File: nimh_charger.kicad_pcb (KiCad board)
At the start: 2 copper layers, 28 parts, among them J1 USB_B_Micro, J2 Bat +, J3 Bat -, Q1 Q_PMOS_DGS, Q2 2N2219, Q3 Q_PMOS_DGS, Q4 Q_PMOS_DGS, U1 LM317L_TO92, U2 LM339

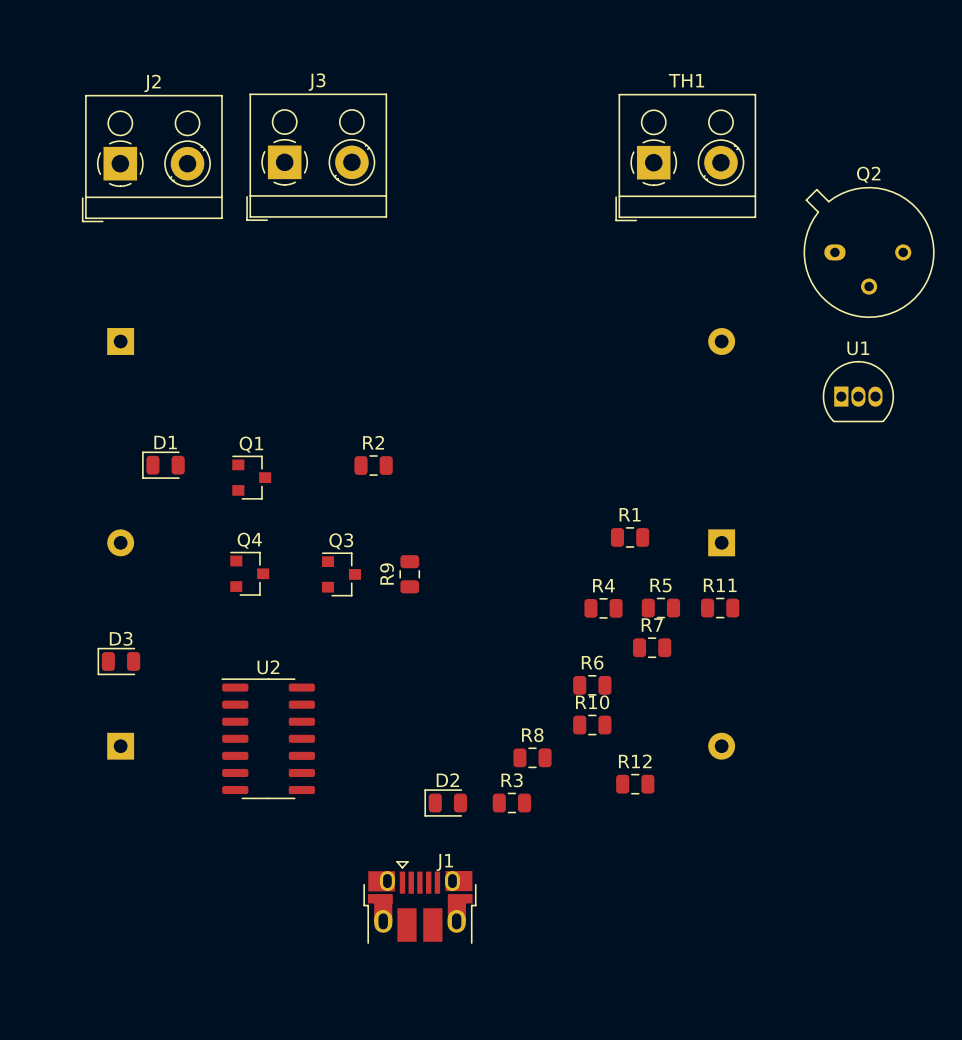
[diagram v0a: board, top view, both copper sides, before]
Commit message: Sorted out some footprints. Working on layout and placement.
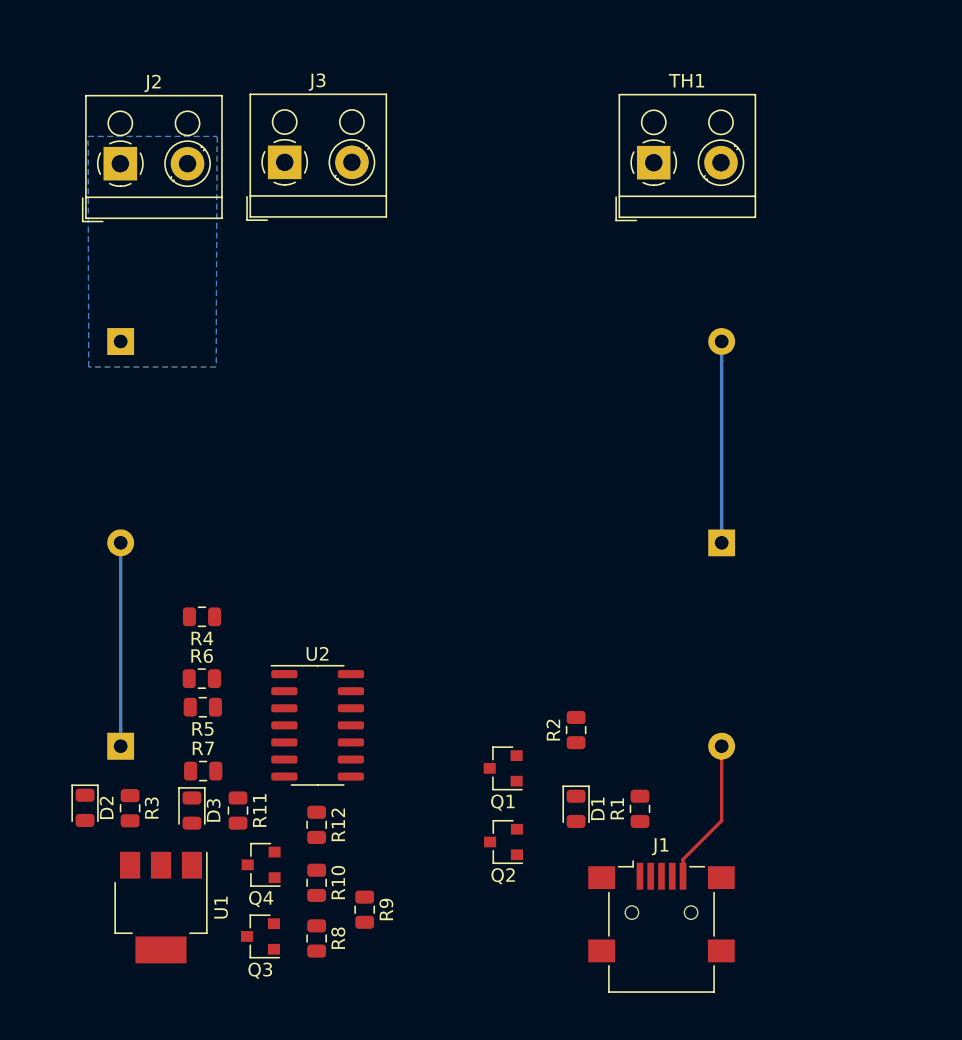
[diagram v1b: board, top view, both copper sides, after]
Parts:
- J1: value USB_B_Micro -> USB_B_Mini; footprint Connector_USB:USB_Micro-B_Amphenol_10103594-0001LF_Horizontal -> Connector_USB:USB_Mini-B_Lumberg_2486_01_Horizontal
- Q2: footprint Package_TO_SOT_THT:TO-39-3 -> Package_TO_SOT_SMD:SOT-23
- U1: value LM317L_TO92 -> LM317_3PinPackage; footprint Package_TO_SOT_THT:TO-92_Inline -> Package_TO_SOT_SMD:SOT-223-3_TabPin2
- moved U1 63.3 mm to (101.2, 115.8), turned to 270 degrees
- moved Q2 50.3 mm to (126.7, 111.0), turned to 180 degrees
- moved D1 39.8 mm to (132.1, 108.5), turned to 270 degrees
- moved R11 38.9 mm to (107.0, 108.6), turned to 270 degrees
- moved R5 34.9 mm to (104.3, 101.0), turned to 180 degrees
- moved R7 34.6 mm to (104.4, 105.7)
- moved R4 29.9 mm to (104.3, 94.2), turned to 180 degrees
- moved R6 29.0 mm to (104.3, 98.8)
- moved Q1 28.6 mm to (126.7, 105.5), turned to 180 degrees
- moved R3 28.4 mm to (98.9, 108.5), turned to 270 degrees
- moved Q3 27.6 mm to (108.6, 118.0), turned to 180 degrees
- moved D2 27.0 mm to (95.6, 108.4), turned to 270 degrees
- moved R9 25.2 mm to (116.4, 116.0), turned to 270 degrees
- moved R2 24.8 mm to (132.1, 102.7), turned to 90 degrees
- moved R12 23.9 mm to (112.8, 109.7), turned to 270 degrees
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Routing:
- net CHR_O: track 0.00 -> 15.1 mm
- net Net-(BT1-Pad2): track 0.00 -> 15.0 mm
- net GNDREF: track 0.00 -> 10.9 mm
- added copper zone on B.Cu, net BAT_V

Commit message: review the design
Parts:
- moved R12 32.2 mm to (133.3, 84.9)
- moved R10 31.8 mm to (133.3, 89.7)
- moved R8 31.8 mm to (133.3, 93.8)
- moved Q3 31.0 mm to (113.9, 87.5)
- moved R11 29.3 mm to (127.5, 87.8)
- moved Q4 28.9 mm to (123.3, 87.8)
- moved R9 28.6 mm to (118.2, 87.5)
- moved D2 18.6 mm to (112.1, 116.9), turned to 90 degrees
- moved U1 16.3 mm to (117.5, 115.6)
- moved R3 13.9 mm to (112.1, 112.8), turned to 90 degrees
- moved D3 12.8 mm to (116.1, 105.9)
- moved Q2 12.1 mm to (136.3, 103.6)
- moved U2 8.09 mm to (119.6, 97.8)
- moved R6 6.73 mm to (110.9, 97.8)
- moved R4 6.72 mm to (110.9, 93.2)
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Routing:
- net BAT_V: track 0.00 -> 87.6 mm, vias 0 -> 2
- net Net-(Q2-Pad2): track 0.00 -> 52.7 mm
- net Net-(D3-Pad2): track 0.00 -> 49.8 mm, vias 0 -> 3
- net +5V: track 0.00 -> 43.8 mm, vias 0 -> 2
- net CHR_O: track 15.1 -> 51.0 mm, vias 0 -> 2
- net Net-(R8-Pad2): track 0.00 -> 34.1 mm, vias 0 -> 2
- net Net-(Q3-Pad3): track 0.00 -> 30.1 mm
- net ~SLOW~: track 0.00 -> 26.8 mm, vias 0 -> 2
- net Net-(Q3-Pad1): track 0.00 -> 22.4 mm
- net Net-(Q1-Pad3): track 0.00 -> 19.8 mm, vias 0 -> 2
- net ~TRK~: track 0.00 -> 16.9 mm, vias 0 -> 2
- net CHG: track 0.00 -> 14.7 mm, vias 0 -> 1
- net Net-(R5-Pad1): track 0.00 -> 9.95 mm
- net Net-(R4-Pad1): track 0.00 -> 9.88 mm
- net GNDREF: track 10.9 -> 20.5 mm, vias 0 -> 5
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- added copper zone on B.Cu, net GNDREF

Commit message: Added some mounting holes
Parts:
- added H1: MountingHole, MountingHole:MountingHole_3mm, F.Cu at (126.1, 60.6)
- added H2: MountingHole, MountingHole:MountingHole_3mm, F.Cu at (97.8, 118.9)
- moved J3 0.10 mm to (110.4, 60.5)
- moved TH1 0.07 mm to (137.9, 60.5)
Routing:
- added copper zone on F.Cu, net Net-(J1-Pad6)
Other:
- board outline added: 52.6 x 67.2 mm
- board text added: "B+"
- board text added: "B-"
- board text added: "NiMH Battery Charger v0.1"
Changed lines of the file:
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@@
   (general
     (thickness 1.6)
-    (drawings 0)
+    (drawings 7)
     (tracks 194)
     (zones 0)
-    (modules 28)
+    (modules 30)
     (nets 23)
   )
@@
     (mod_text_size 1 1)
     (mod_text_width 0.15)
-    (pad_size 1.524 1.524)
-    (pad_drill 0.762)
+    (pad_size 3 3)
+    (pad_drill 3)
     (pad_to_mask_clearance 0.051)
     (solder_mask_min_width 0.25)
@@
     (descr "terminal block RND 205-00001, 2 pins, pitch 5mm, size 10x9mm^2, drill diamater 1.3mm, pad diameter 2.5mm, see http://cdn-reichelt.de/documents/datenblatt/C151/RND_205-00001_DB_EN.pdf, script-generated using https://github.com/pointhi/kicad-footprint-generator/scripts/TerminalBlock_RND")
     (tags "THT terminal block RND 205-00001 pitch 5mm size 10x9mm^2 drill 1.3mm pad 2.5mm")
-    (fp_text reference J2 (at 2.5 -6.06) (layer F.SilkS)
+    (fp_text reference J2 (at 2.5 5.525) (layer F.SilkS)
       (effects (font (size 1 1) (thickness 0.15)))
     )
@@
   )
   (module TerminalBlock_RND:TerminalBlock_RND_205-00001_1x02_P5.00mm_Horizontal (layer F.Cu)
-    (at 110.425 60.425)
+    (at 110.425 60.525)
     (descr "terminal block RND 205-00001, 2 pins, pitch 5mm, size 10x9mm^2, drill diamater 1.3mm, pad diameter 2.5mm, see http://cdn-reichelt.de/documents/datenblatt/C151/RND_205-00001_DB_EN.pdf, script-generated using https://github.com/pointhi/kicad-footprint-generator/scripts/TerminalBlock_RND")
     (tags "THT terminal block RND 205-00001 pitch 5mm size 10x9mm^2 drill 1.3mm pad 2.5mm")
-    (fp_text reference J3 (at 2.5 -6.06) (layer F.SilkS)
+    (fp_text reference J3 (at 2.5 5.6) (layer F.SilkS)
       (effects (font (size 1 1) (thickness 0.15)))
     )
@@
   )
   (module TerminalBlock_RND:TerminalBlock_RND_205-00001_1x02_P5.00mm_Horizontal (layer F.Cu)
-    (at 137.875 60.45)
+    (at 137.875 60.525)
     (descr "terminal block RND 205-00001, 2 pins, pitch 5mm, size 10x9mm^2, drill diamater 1.3mm, pad diameter 2.5mm, see http://cdn-reichelt.de/documents/datenblatt/C151/RND_205-00001_DB_EN.pdf, script-generated using https://github.com/pointhi/kicad-footprint-generator/scripts/TerminalBlock_RND")
     (tags "THT terminal block RND 205-00001 pitch 5mm size 10x9mm^2 drill 1.3mm pad 2.5mm")
-    (fp_text reference TH1 (at 2.5 -6.06) (layer F.SilkS)
+    (fp_text reference TH1 (at 2.525 5.525) (layer F.SilkS)
       (effects (font (size 1 1) (thickness 0.15)))
     )
@@
     )
   )
+  (module MountingHole:MountingHole_3mm (layer F.Cu)
+    (at 126.1 60.625)
+    (descr "Mounting Hole 3mm, no annular")
+    (tags "mounting hole 3mm no annular")
+    (attr virtual)
+    (fp_text reference H1 (at 0 -4) (layer F.SilkS)
+      (effects (font (size 1 1) (thickness 0.15)))
+    )
+    (fp_text value MountingHole (at 0 4) (layer F.Fab)
+      (effects (font (size 1 1) (thickness 0.15)))
+    )
+    (fp_text user %R (at 0.3 0) (layer F.Fab)
+      (effects (font (size 1 1) (thickness 0.15)))
+    )
+    (fp_circle (center 0 0) (end 3 0) (layer Cmts.User) (width 0.15))
+    (fp_circle (center 0 0) (end 3.25 0) (layer F.CrtYd) (width 0.05))
+    (pad "" np_thru_hole circle (at 0 -0.1) (size 3 3) (drill 3) (layers *.Cu *.Mask))
+  )
+  (module MountingHole:MountingHole_3mm (layer F.Cu)
+    (at 97.825 118.925)
+    (descr "Mounting Hole 3mm, no annular")
+    (tags "mounting hole 3mm no annular")
+    (attr virtual)
+    (fp_text reference H2 (at 0 -4) (layer F.SilkS)
+      (effects (font (size 1 1) (thickness 0.15)))
+    )
+    (fp_text value MountingHole (at 0 4) (layer F.Fab)
+      (effects (font (size 1 1) (thickness 0.15)))
+    )
+    (fp_circle (center 0 0) (end 3.25 0) (layer F.CrtYd) (width 0.05))
+    (fp_circle (center 0 0) (end 3 0) (layer Cmts.User) (width 0.15))
+    (fp_text user %R (at 0.3 0) (layer F.Fab)
+      (effects (font (size 1 1) (thickness 0.15)))
+    )
+    (pad 1 np_thru_hole circle (at 0 0) (size 3 3) (drill 3) (layers *.Cu *.Mask))
+  )
+  (gr_text "NiMH Battery Charger\nv0.1" (at 120.975 77.025) (layer F.SilkS)
+    (effects (font (size 1 1) (thickness 0.15)))
+  )
+  (gr_text B- (at 112.925 68.425) (layer F.SilkS)
+    (effects (font (size 3 3) (thickness 0.15)))
+  )
+  (gr_text B+ (at 100.35 68.425) (layer F.SilkS)
+    (effects (font (size 3 3) (thickness 0.15)))
+  )
+  (gr_line (start 147.05 55) (end 147.05 122.25) (layer Edge.Cuts) (width 0.05))
+  (gr_line (start 94.5 55) (end 147.05 55) (layer Edge.Cuts) (width 0.05))
+  (gr_line (start 94.5 122.25) (end 94.5 55) (layer Edge.Cuts) (width 0.05))
+  (gr_line (start 147.05 122.25) (end 94.5 122.25) (layer Edge.Cuts) (width 0.05))
   (via (at 114.95 99.075) (size 0.8) (drill 0.4) (layers F.Cu B.Cu) (net 1))
   (segment (start 117.125 99.07) (end 114.955 99.07) (width 0.25) (layer F.Cu) (net 1))
@@
       )
     )
+  )
+  (zone (net 9) (net_name "Net-(J1-Pad6)") (layer F.Cu) (hatch edge 0.508)
+    (connect_pads (clearance 0.508))
+    (min_thickness 0.254)
+    (fill yes (arc_segments 32) (thermal_gap 0.508) (thermal_bridge_width 0.508))
+    (polygon
+      (pts
+        (xy 144.325 120.875) (xy 132.1 120.875) (xy 132.1 112) (xy 135.375 112) (xy 135.4 117.775)
+        (xy 141.575 117.65) (xy 141.575 111.85) (xy 144.325 111.775)
+      )
+    )
